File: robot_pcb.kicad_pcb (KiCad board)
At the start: 2 copper layers, 140 x 180 mm, 190 parts, among them J1 Raspberry_Pi_2_3, J10 Servo_TrayRelease, J14 Motor FR, J17 Conn_01x04, J18 USB_C_Receptacle_PowerOnly_6P, J2 Power_Bypass, J23 Motor BR, J25 ConductClaw, J26 Motor BL, J27 TOF_Front, J28 OLED_Display, J29 Motor FL, J3 Lipo, J6 TOF_Claw, J7 UltraS_Side, J8 Servo_Grab, J9 Servo_Lift, Q2 Q_NMOS_GDS, SW1 SW_SPDT, SW2 SW_Push, U1 STM32F407VGTx, U10 DMG2305UX-7, U11 DMG2305UX-7, U2 BQ76920PW, U3 AP64501SP-13, U4 MAX25240AFFD/VY+, U5 DMG2305UX-7, U6 AP64501SP-13, U7 AP64501SP-13, U9 BNO086, Y1 25MHz, Y2 32.768kHz

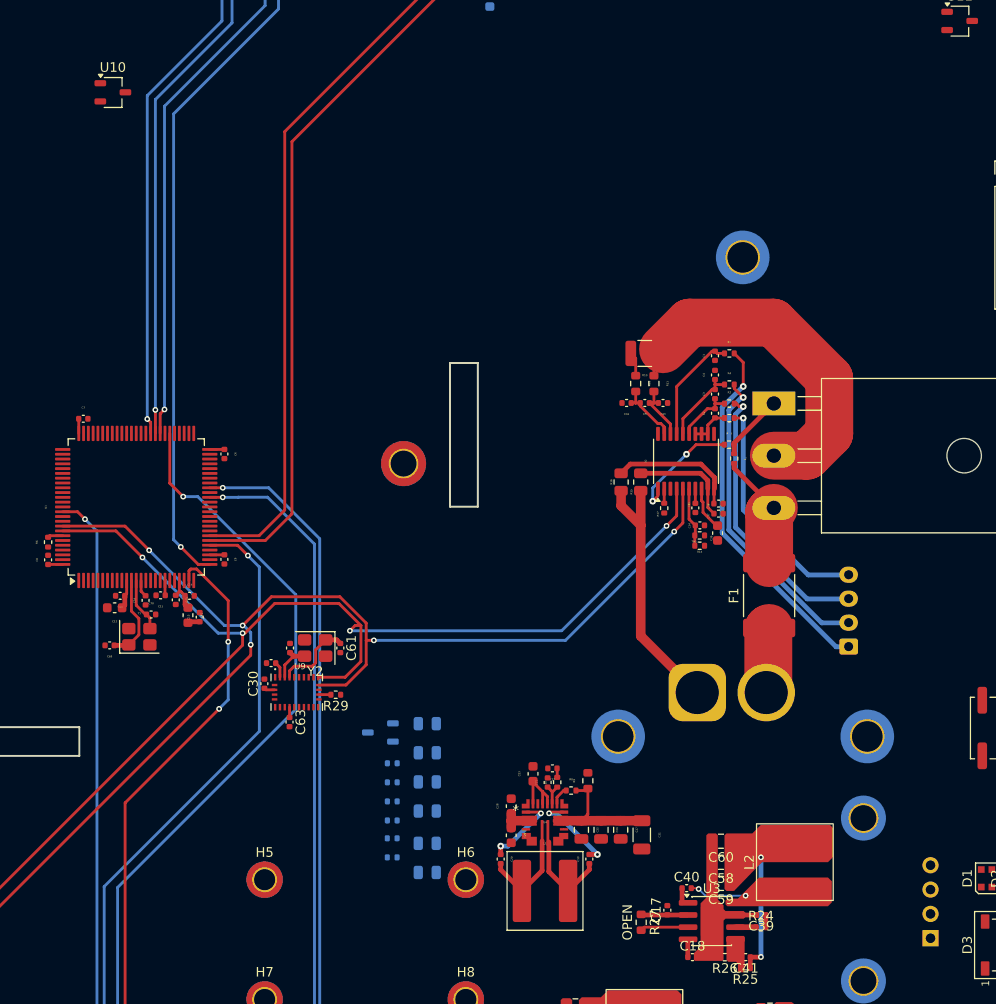
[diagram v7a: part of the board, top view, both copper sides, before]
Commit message: moved ultrasonic
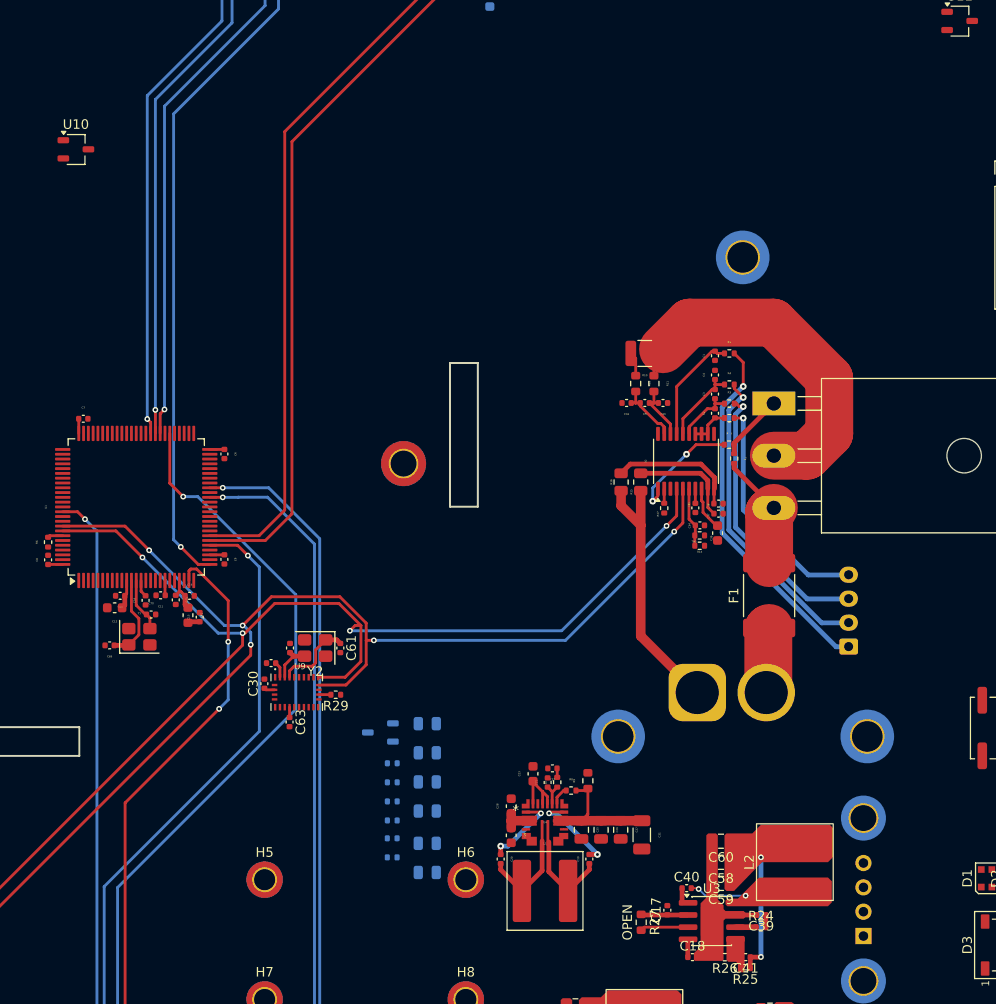
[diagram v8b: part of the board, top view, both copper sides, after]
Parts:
- J17: value Conn_01x04 -> Programmer
- moved U10 7.09 mm to (73.2, 77.9)
- moved J7 7.00 mm to (155.4, 160.0)
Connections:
- J7 pad 4: unconnected-(J7-Pin_4-Pad4) -> +5V
